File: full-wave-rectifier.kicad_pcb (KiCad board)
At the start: 2 copper layers, 80.6 x 108 mm, 67 parts, among them J10 Control Right, J11 Main Right, J12 Power Connector, J2 Input Ch1, J3 Input Ch2, J4 Output Ch1, J5 Output Ch2, J6 Ochd input, J8 Control Left, J9 Main Left, Q7 AO3404A, Q8 AO3407A, U2 TL074, U3 TL074, U4 TL074, U5 LM4040DBZ-5

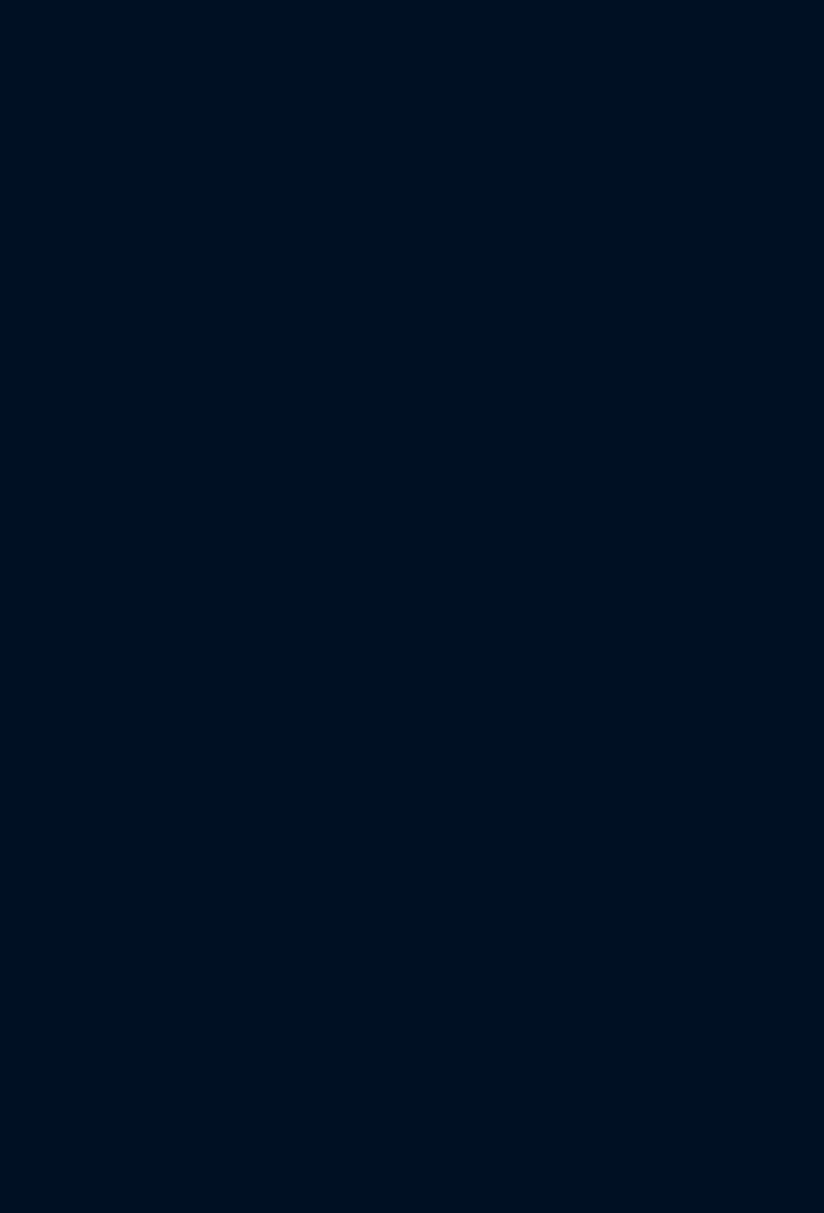
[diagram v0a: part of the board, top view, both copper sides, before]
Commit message: feat: add Eurorack jack and LED footprints to PCB
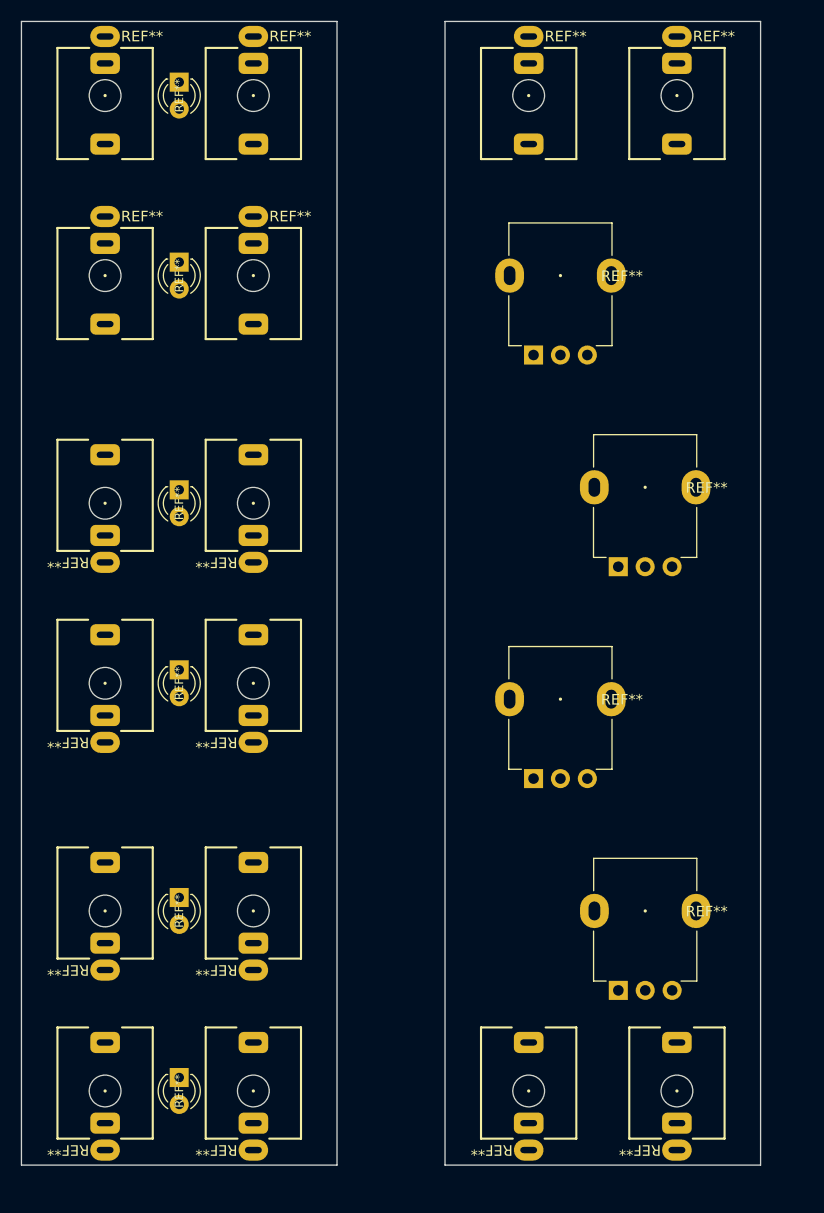
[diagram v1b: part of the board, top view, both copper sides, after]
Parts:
- added REF**: WQP518MA, Eurorack:Jack_3.5mm_WQP518MA_2, F.Cu at (43.0, 70.0)
- added REF**: WQP518MA, Eurorack:Jack_3.5mm_WQP518MA_2, F.Cu at (97.0, 53.0)
- added REF**: WQP518MA, Eurorack:Jack_3.5mm_WQP518MA_2, F.Cu at (57.0, 108.5)
- added REF**: WQP518MA, Eurorack:Jack_3.5mm_WQP518MA_2, F.Cu at (83.0, 147.0)
- added REF**: WQP518MA, Eurorack:Jack_3.5mm_WQP518MA_2, F.Cu at (43.0, 130.0)
- added REF**: LED_D3.0mm, Eurorack:LED_D3.0mm, F.Cu at (50.0, 90.2)
- added REF**: WQP518MA, Eurorack:Jack_3.5mm_WQP518MA_2, F.Cu at (57.0, 130.0)
- added REF**: WQP518MA, Eurorack:Jack_3.5mm_WQP518MA_2, F.Cu at (57.0, 70.0)
- added REF**: LED_D3.0mm, Eurorack:LED_D3.0mm, F.Cu at (50.0, 51.7)
- added REF**: WQP518MA, Eurorack:Jack_3.5mm_WQP518MA_2, F.Cu at (97.0, 147.0)
- added REF**: Pot_Alpha_9mm, AudioPots:RD901F, F.Cu at (94.0, 90.0)
- added REF**: WQP518MA, Eurorack:Jack_3.5mm_WQP518MA_2, F.Cu at (57.0, 53.0)
- added REF**: LED_D3.0mm, Eurorack:LED_D3.0mm, F.Cu at (50.0, 145.7)
- added REF**: WQP518MA, Eurorack:Jack_3.5mm_WQP518MA_2, F.Cu at (43.0, 108.5)
- added REF**: WQP518MA, Eurorack:Jack_3.5mm_WQP518MA_2, F.Cu at (57.0, 147.0)
- added REF**: WQP518MA, Eurorack:Jack_3.5mm_WQP518MA_2, F.Cu at (43.0, 147.0)
- added REF**: WQP518MA, Eurorack:Jack_3.5mm_WQP518MA_2, F.Cu at (83.0, 53.0)
- added REF**: LED_D3.0mm, Eurorack:LED_D3.0mm, F.Cu at (50.0, 68.7)
- added REF**: Pot_Alpha_9mm, AudioPots:RD901F, F.Cu at (94.0, 130.0)
- added REF**: LED_D3.0mm, Eurorack:LED_D3.0mm, F.Cu at (50.0, 128.7)
- added REF**: Pot_Alpha_9mm, AudioPots:RD901F, F.Cu at (86.0, 110.0)
- added REF**: WQP518MA, Eurorack:Jack_3.5mm_WQP518MA_2, F.Cu at (43.0, 53.0)
- added REF**: Pot_Alpha_9mm, AudioPots:RD901F, F.Cu at (86.0, 70.0)
- added REF**: LED_D3.0mm, Eurorack:LED_D3.0mm, F.Cu at (50.0, 107.2)
- added REF**: WQP518MA, Eurorack:Jack_3.5mm_WQP518MA_2, F.Cu at (43.0, 91.5)
- added REF**: WQP518MA, Eurorack:Jack_3.5mm_WQP518MA_2, F.Cu at (57.0, 91.5)
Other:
- board size 80.6 x 108 mm -> 157.6 x 110.5 mm
